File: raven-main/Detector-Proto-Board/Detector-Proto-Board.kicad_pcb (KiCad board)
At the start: 2 copper layers, 40.2 x 40.4 mm, 41 parts, among them IC1 ADA4817-1ARDZ-R7, J1 Conn_01x04, J2 Conn_01x01, J3 Conn_01x02, U9 TLV3201AIDCKT

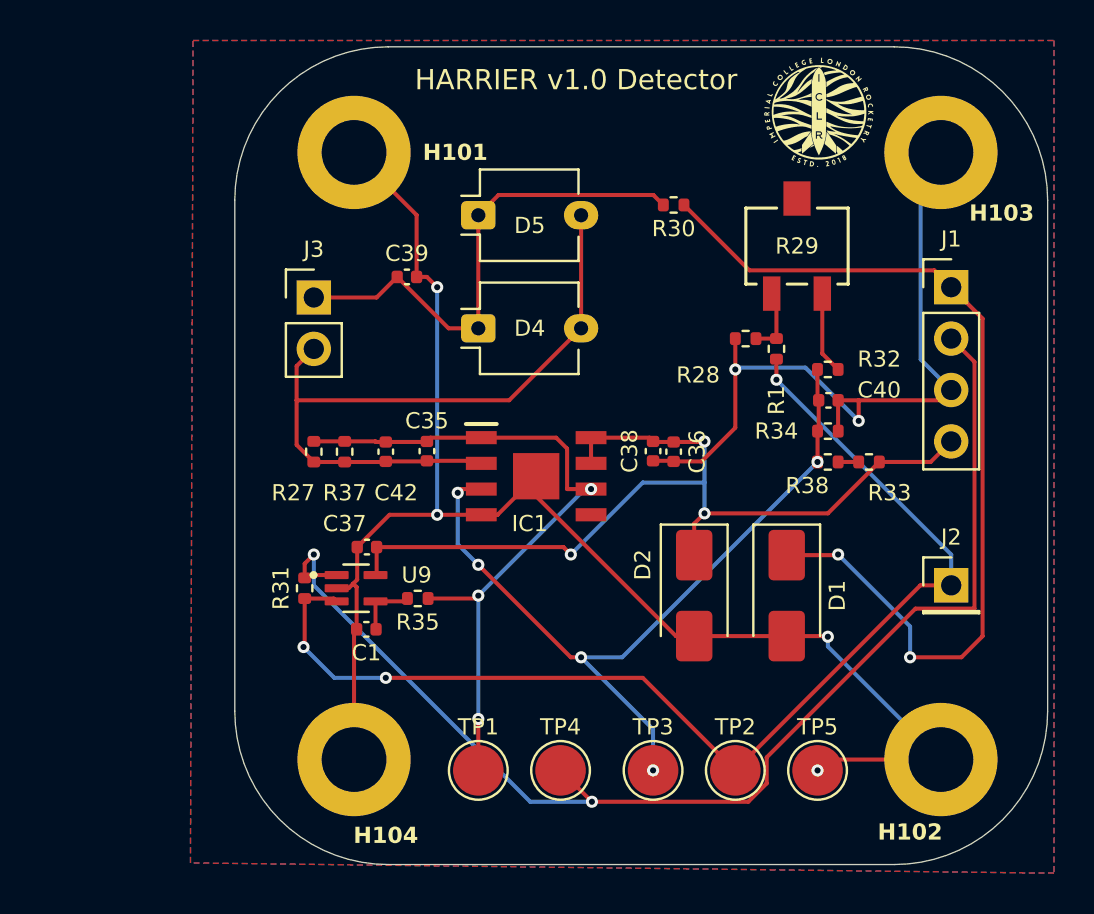
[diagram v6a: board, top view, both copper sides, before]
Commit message: Repositioned TVS diode
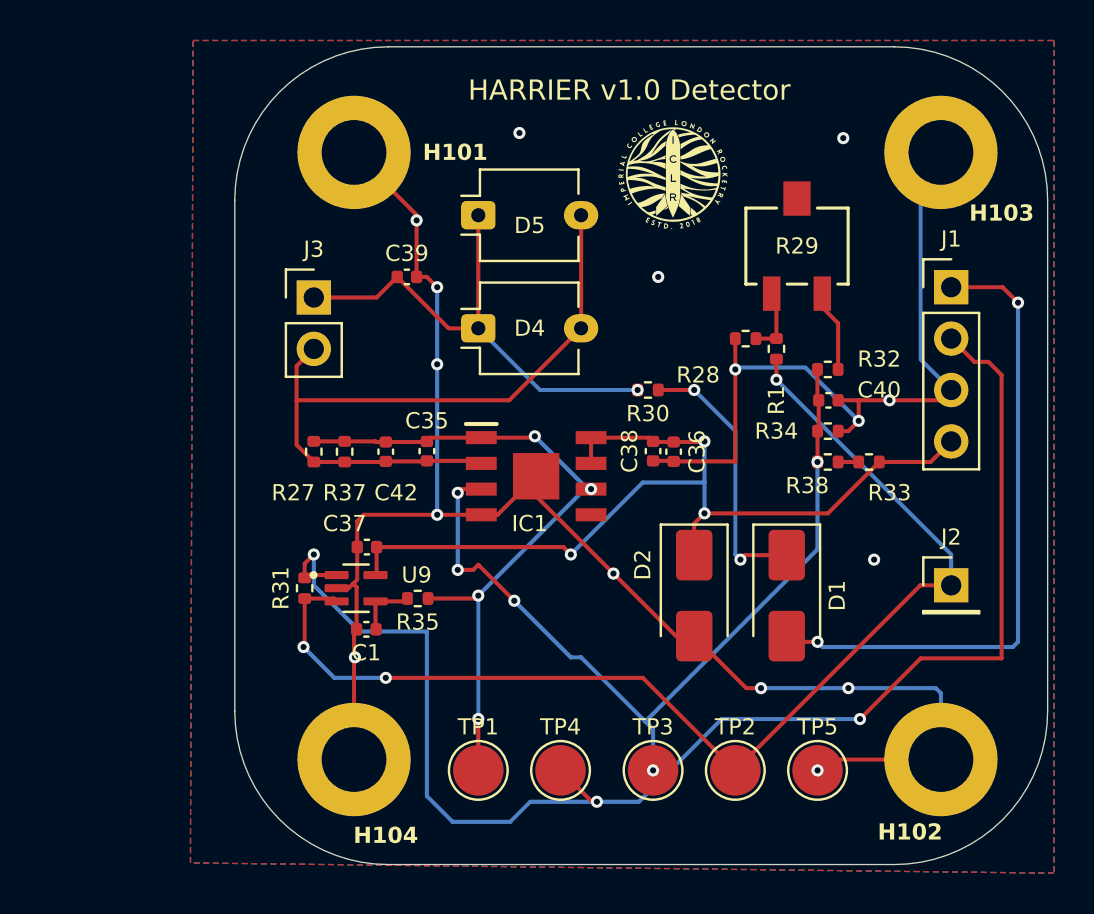
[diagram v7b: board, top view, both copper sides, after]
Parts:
- moved R30 9.23 mm to (112.5, 78.7)
- moved G*** 7.84 mm to (113.8, 68.1)
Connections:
- D1 pad 2: GND -> Net-(D1-A2)
- J1 pad 1: +25V -> Net-(D1-A2)
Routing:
- net +25V: track 45.9 -> 13.5 mm
- net Net-(D1-A2): track 0.00 -> 32.1 mm, vias 0 -> 2
- net /Detector_Out_A: track 62.3 -> 70.9 mm, vias 2 -> 3
- net GND: track 111.9 -> 115.0 mm, vias 6 -> 16
- net /Vped: track 39.6 -> 41.2 mm
- net /OUT: track 35.3 -> 34.1 mm, vias 3 -> 4
- net Net-(D4-K): track 24.9 -> 24.3 mm, vias 0 -> 1

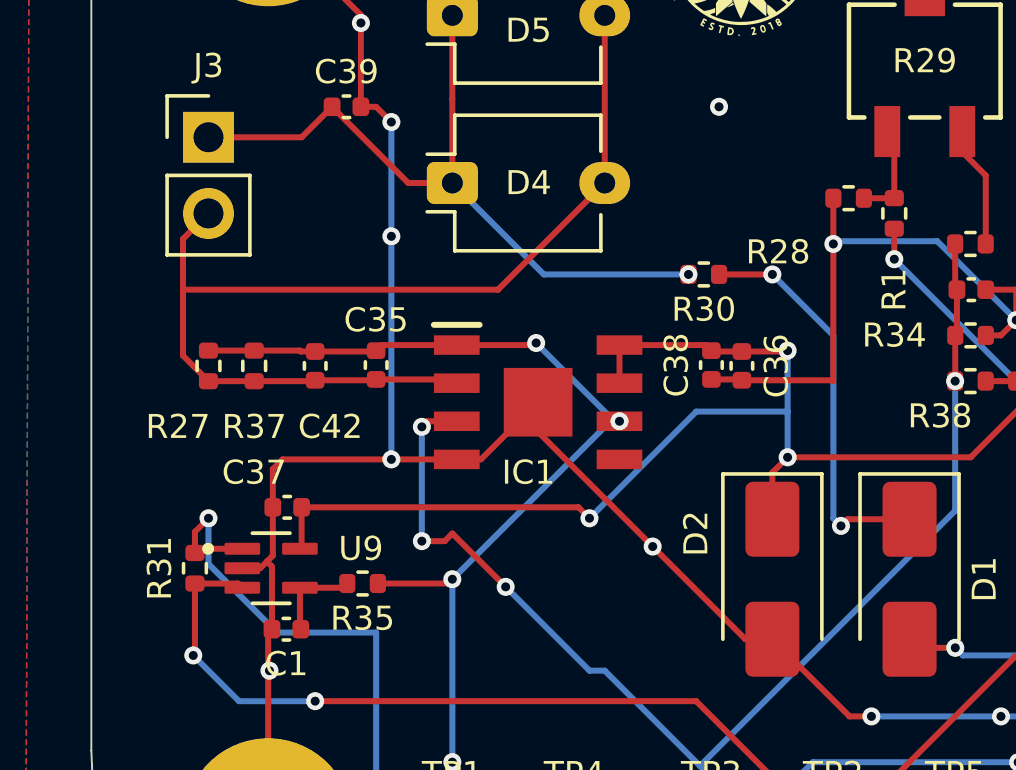
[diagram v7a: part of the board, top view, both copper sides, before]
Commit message: Seperated touching lines
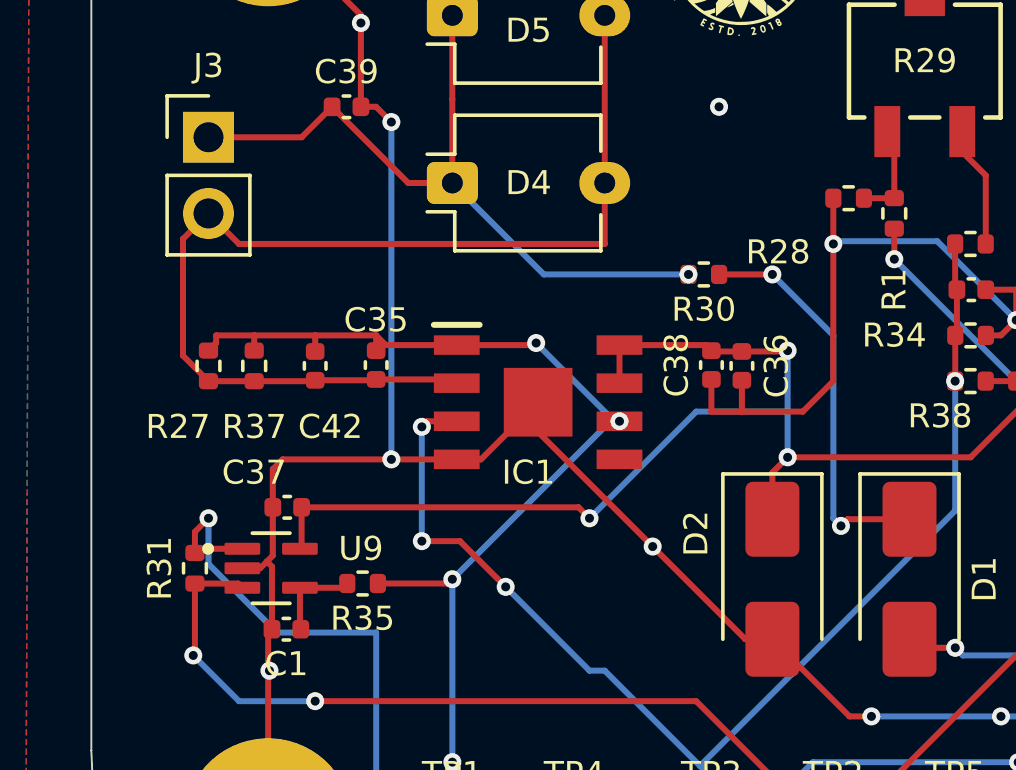
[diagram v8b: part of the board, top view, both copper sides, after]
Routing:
- net GND: track 115.0 -> 117.5 mm, vias 16 -> 15
- net /OUT: track 34.1 -> 36.4 mm
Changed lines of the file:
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@@
 	)
 	(segment
-		(start 95.162 79.248)
-		(end 105.664 79.248)
+		(start 109.22 77.724)
+		(end 109.22 75.692)
+		(width 0.2)
+		(layer "F.Cu")
+		(net "Net-(D4-A)")
+	)
+	(segment
+		(start 96.012 76.708)
+		(end 97.028 77.724)
 		(width 0.2)
 		(layer "F.Cu")
@@
 	)
 	(segment
-		(start 105.664 79.248)
-		(end 109.22 75.692)
-		(width 0.2)
-		(layer "F.Cu")
-		(net "Net-(D4-A)")
-	)
-	(segment
 		(start 109.22 70.104)
 		(end 109.22 75.692)
@@
 	)
 	(segment
+		(start 97.028 77.724)
+		(end 109.22 77.724)
+		(width 0.2)
+		(layer "F.Cu")
+		(net "Net-(D4-A)")
+	)
+	(segment
 		(start 96.012 82.298)
 		(end 97.536 82.298)
@@
 	)
 	(segment
-		(start 99.568 81.308)
-		(end 101.572 81.308)
+		(start 96.266 81.024)
+		(end 96.012 81.278)
 		(width 0.2)
 		(layer "F.Cu")
@@
 	)
 	(segment
+		(start 96.266 80.772)
+		(end 96.266 81.024)
+		(width 0.2)
+		(layer "F.Cu")
+		(net "/OUT")
+	)
+	(segment
 		(start 103.998 89.042)
 		(end 101.658 89.042)
@@
 	)
 	(segment
+		(start 97.536 80.772)
+		(end 99.568 80.772)
+		(width 0.2)
+		(layer "F.Cu")
+		(net "/OUT")
+	)
+	(segment
 		(start 104.14 97.536)
 		(end 104.14 94.996)
@@
 	)
 	(segment
-		(start 104.288 81.095)
-		(end 101.785 81.095)
-		(width 0.2)
-		(layer "F.Cu")
-		(net "/OUT")
-	)
-	(segment
-		(start 96.012 81.278)
-		(end 97.536 81.278)
+		(start 101.6 80.772)
+		(end 101.6 81.28)
 		(width 0.2)
 		(layer "F.Cu")
@@
 	)
 	(segment
-		(start 99.568 81.308)
-		(end 99.088 81.308)
-		(width 0.2)
-		(layer "F.Cu")
-		(net "/OUT")
-	)
-	(segment
-		(start 99.058 81.278)
-		(end 97.536 81.278)
-		(width 0.2)
-		(layer "F.Cu")
-		(net "/OUT")
-	)
-	(segment
-		(start 99.088 81.308)
-		(end 99.058 81.278)
+		(start 101.923 81.095)
+		(end 104.288 81.095)
+		(width 0.2)
+		(layer "F.Cu")
+		(net "/OUT")
+	)
+	(segment
+		(start 99.568 80.772)
+		(end 101.6 80.772)
+		(width 0.2)
+		(layer "F.Cu")
+		(net "/OUT")
+	)
+	(segment
+		(start 97.536 80.772)
+		(end 96.266 80.772)
+		(width 0.2)
+		(layer "F.Cu")
+		(net "/OUT")
+	)
+	(segment
+		(start 101.6 80.772)
+		(end 101.923 81.095)
+		(width 0.2)
+		(layer "F.Cu")
+		(net "/OUT")
+	)
+	(segment
+		(start 97.536 81.278)
+		(end 97.536 80.772)
+		(width 0.2)
+		(layer "F.Cu")
+		(net "/OUT")
+	)
+	(segment
+		(start 99.568 80.772)
+		(end 99.568 81.308)
 		(width 0.2)
 		(layer "F.Cu")
@@
 	)
 	(segment
-		(start 104.14 87.376)
-		(end 105.918 89.154)
-		(width 0.2)
-		(layer "F.Cu")
-		(net "/Vped")
-	)
-	(segment
 		(start 104.288 83.635)
 		(end 103.309 83.635)
@@
 	)
 	(segment
-		(start 103.886 87.63)
-		(end 104.14 87.376)
+		(start 104.394 87.63)
+		(end 105.918 89.154)
 		(width 0.2)
 		(layer "F.Cu")
@@
 	(segment
 		(start 103.124 87.63)
-		(end 103.886 87.63)
+		(end 104.394 87.63)
 		(width 0.2)
 		(layer "F.Cu")
@@
 	)
 	(segment
+		(start 115.824 83.312)
+		(end 116.84 82.296)
+		(width 0.2)
+		(layer "F.Cu")
+		(net "GND")
+	)
+	(segment
 		(start 102.108 84.905)
 		(end 98.483 84.905)
@@
 	)
 	(segment
-		(start 116.812 82.268)
-		(end 116.84 82.296)
+		(start 112.776 83.312)
+		(end 113.792 83.312)
 		(width 0.2)
 		(layer "F.Cu")
@@
 	)
 	(segment
+		(start 113.792 83.312)
+		(end 115.824 83.312)
+		(width 0.2)
+		(layer "F.Cu")
+		(net "GND")
+	)
+	(segment
 		(start 114.808 90.9)
 		(end 113.908 90.9)
@@
 	)
 	(segment
-		(start 112.776 82.24)
-		(end 113.764 82.24)
-		(width 0.2)
-		(layer "F.Cu")
-		(net "GND")
-	)
-	(segment
 		(start 122.428 80.772)
 		(end 122.936 80.264)
@@
 	)
 	(segment
+		(start 113.792 83.312)
+		(end 113.792 82.268)
+		(width 0.2)
+		(layer "F.Cu")
+		(net "GND")
+	)
+	(segment
 		(start 114.808 90.9)
 		(end 117.38 93.472)
@@
 	)
 	(segment
-		(start 113.792 82.268)
-		(end 116.812 82.268)
-		(width 0.2)
-		(layer "F.Cu")
-		(net "GND")
-	)
-	(segment
 		(start 121.44 97)
 		(end 120.904 97.536)
@@
 	)
 	(segment
+		(start 112.776 82.24)
+		(end 112.776 83.312)
+		(width 0.2)
+		(layer "F.Cu")
+		(net "GND")
+	)
+	(segment
 		(start 113.908 90.9)
 		(end 107 83.992)
@@
 	)
 	(via
-		(at 102.108 77.47)
-		(size 0.6)
-		(drill 0.3)
-		(layers "F.Cu" "B.Cu")
-		(net "GND")
-	)
-	(via
 		(at 122.428 93.472)
 		(size 0.6)
@@
 	)
 	(segment
+		(start 117.094 87.122)
+		(end 117.316 86.9)
+		(width 0.2)
+		(layer "F.Cu")
+		(net "+25V")
+	)
+	(segment
+		(start 113.032 78.74)
+		(end 114.808 78.74)
+		(width 0.2)
+		(layer "F.Cu")
+		(net "+25V")
+	)
+	(segment
 		(start 117.316 86.9)
 		(end 119.38 86.9)
 		(width 0.2)
 		(layer "F.Cu")
-		(net "+25V")
-	)
-	(segment
-		(start 113.032 78.74)
-		(end 114.808 78.74)
-		(width 0.2)
-		(layer "F.Cu")
-		(net "+25V")
-	)
-	(segment
-		(start 117.094 87.122)
-		(end 117.316 86.9)
-		(width 0.2)
-		(layer "F.Cu")
